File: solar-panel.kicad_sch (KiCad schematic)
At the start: 2 parts, among them U501 MCP3008

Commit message: solar panel init
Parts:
- renumbered U501 to U101
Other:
- added sheet Solar Cells (pv_cells.kicad_sch)
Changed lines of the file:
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@@
     (stroke (width 0) (type default))
-  )
-  (rectangle (start 102.87 53.34) (end 165.1 115.57)
-    (stroke (width 0) (type default))
-    (fill (type none))
   )
   (text "ADC\n" (at 118.11 71.12 0)
@@
   (symbol (lib_id "Analog_ADC:MCP3008") (at 129.54 91.44 0) (unit 1)
     (in_bom yes) (on_board yes) (dnp no) (fields_autoplaced)
-    (property "Reference" "U501" (at 124.3583 107.1499 0)
+    (property "Reference" "U101" (at 124.3583 107.1499 0)
       (effects (font (size 1.27 1.27)) (justify right))
     )
@@
       )
     )
+  )
+  (sheet (at 166.37 52.07) (size 35.56 5.08) (fields_autoplaced)
+    (stroke (width 0.1524) (type solid))
+    (fill (color 199 255 204 1.0000))
+    (property "Sheetname" "Solar Cells" (at 166.37 51.3584 0)
+      (effects (font (size 1.27 1.27)) (justify left bottom))
+    )
+    (property "Sheetfile" "pv_cells.kicad_sch" (at 166.37 57.7346 0)
+      (effects (font (size 1.27 1.27)) (justify left top))
+    )
+    (pin "PV_V+" output (at 201.93 54.61 0)
+      (effects (font (size 1.27 1.27)) (justify right))
+    )
+    (pin "PV_V-" input (at 166.37 54.61 180)
+      (effects (font (size 1.27 1.27)) (justify left))
+    )
+    (instances
+      (project "solar-panel"
+        (path "/3cfd2153-52bb-4eed-95c6-13d99c50d08a" (page "6"))
+      )
+    )

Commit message: rev 1.0, added pdf
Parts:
- added J101: Conn_01x10, Connector_PinSocket_1.00mm:PinSocket_1x10_P1.00mm_Vertical, symbol Connector_Generic:Conn_01x10
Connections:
- net MISO: now also J101.3 (Pin_3)
- net MOSI: now also J101.2 (Pin_2)
- net SCK: now also J101.1 (Pin_1)
- net Solar Cells/PV_V+: now also J101.10 (Pin_10), J101.8 (Pin_8), J101.9 (Pin_9)
- net Solar Cells/PV_V-: now also J101.5 (Pin_5), J101.6 (Pin_6), J101.7 (Pin_7)
- net ~{CS}: now also J101.4 (Pin_4)
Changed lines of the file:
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@@
 (kicad_sch (version 20230121) (generator eeschema)
   (paper "A4")
+  (junction (at 171.45 104.14) (diameter 0) (color 0 0 0 0)
+  )
   (junction (at 134.62 78.74) (diameter 0) (color 0 0 0 0)
   )
+  (junction (at 171.45 106.68) (diameter 0) (color 0 0 0 0)
+  )
   (junction (at 130.81 106.68) (diameter 0) (color 0 0 0 0)
+  )
+  (junction (at 171.45 109.22) (diameter 0) (color 0 0 0 0)
+  )
+  (junction (at 171.45 101.6) (diameter 0) (color 0 0 0 0)
   )
   (junction (at 134.62 63.5) (diameter 0) (color 0 0 0 0)
@@
   (no_connect (at 114.3 99.06))
   (no_connect (at 114.3 93.98))
-  (wire (pts (xy 149.86 96.52) (xy 144.78 96.52))
+  (wire (pts (xy 171.45 106.68) (xy 171.45 109.22))
+    (stroke (width 0) (type default))
+  )
+  (wire (pts (xy 144.78 96.52) (xy 171.45 96.52))
     (stroke (width 0) (type default))
   )
@@
     (stroke (width 0) (type default))
   )
+  (wire (pts (xy 144.78 88.9) (xy 171.45 88.9))
+    (stroke (width 0) (type default))
+  )
+  (wire (pts (xy 158.75 104.14) (xy 171.45 104.14))
+    (stroke (width 0) (type default))
+  )
   (wire (pts (xy 130.81 106.68) (xy 134.62 106.68))
     (stroke (width 0) (type default))
@@
     (stroke (width 0) (type default))
   )
+  (wire (pts (xy 171.45 109.22) (xy 171.45 111.76))
+    (stroke (width 0) (type default))
+  )
+  (wire (pts (xy 158.75 106.68) (xy 171.45 106.68))
+    (stroke (width 0) (type default))
+  )
   (wire (pts (xy 86.36 76.2) (xy 114.3 76.2))
     (stroke (width 0) (type default))
@@
     (stroke (width 0) (type default))
   )
-  (wire (pts (xy 149.86 88.9) (xy 144.78 88.9))
-    (stroke (width 0) (type default))
-  )
   (wire (pts (xy 134.62 63.5) (xy 139.7 63.5))
     (stroke (width 0) (type default))
   )
-  (wire (pts (xy 149.86 93.98) (xy 144.78 93.98))
+  (wire (pts (xy 144.78 93.98) (xy 171.45 93.98))
+    (stroke (width 0) (type default))
+  )
+  (wire (pts (xy 171.45 99.06) (xy 171.45 101.6))
+    (stroke (width 0) (type default))
+  )
+  (wire (pts (xy 171.45 101.6) (xy 171.45 104.14))
     (stroke (width 0) (type default))
   )
@@
     (stroke (width 0) (type default))
   )
-  (wire (pts (xy 149.86 91.44) (xy 144.78 91.44))
+  (wire (pts (xy 144.78 91.44) (xy 171.45 91.44))
     (stroke (width 0) (type default))
   )
@@
     )
   )
+  (symbol (lib_id "Connector_Generic:Conn_01x10") (at 176.53 99.06 0) (unit 1)
+    (in_bom yes) (on_board yes) (dnp no) (fields_autoplaced)
+    (property "Reference" "J101" (at 178.562 99.6863 0)
+      (effects (font (size 1.27 1.27)) (justify left))
+    )
+    (property "Value" "Conn_01x10" (at 178.562 101.6073 0)
+      (effects (font (size 1.27 1.27)) (justify left))
+    )
+    (property "Footprint" "Connector_PinSocket_1.00mm:PinSocket_1x10_P1.00mm_Vertical" (at 176.53 99.06 0)
+      (effects (font (size 1.27 1.27)) hide)
+    )
+    (property "Datasheet" "~" (at 176.53 99.06 0)
+      (effects (font (size 1.27 1.27)) hide)
+    )
+    (pin "1")
+    (pin "10")
+    (pin "2")
+    (pin "3")
+    (pin "4")
+    (pin "5")
+    (pin "6")
+    (pin "7")
+    (pin "8")
+    (pin "9")
+    (instances
+      (project "solar-panel"
+        (path "/3cfd2153-52bb-4eed-95c6-13d99c50d08a"
+          (reference "J101") (unit 1)
+        )
+      )
+    )
+  )
   (sheet (at 68.58 83.82) (size 17.78 4.699)
     (stroke (width 0.1524) (type solid))
@@
     )
   )
-  (sheet (at 166.37 52.07) (size 35.56 5.08) (fields_autoplaced)
+  (sheet (at 146.05 101.6) (size 12.7 7.62) (fields_autoplaced)
     (stroke (width 0.1524) (type solid))
     (fill (color 199 255 204 1.0000))
-    (property "Sheetname" "Solar Cells" (at 166.37 51.3584 0)
+    (property "Sheetname" "Solar Cells" (at 146.05 100.8884 0)
       (effects (font (size 1.27 1.27)) (justify left bottom))
     )
-    (property "Sheetfile" "pv_cells.kicad_sch" (at 166.37 57.7346 0)
+    (property "Sheetfile" "pv_cells.kicad_sch" (at 146.05 109.8046 0)
       (effects (font (size 1.27 1.27)) (justify left top))
     )
-    (pin "PV_V+" output (at 201.93 54.61 0)
-      (effects (font (size 1.27 1.27)) (justify right))
-    )
-    (pin "PV_V-" input (at 166.37 54.61 180)
-      (effects (font (size 1.27 1.27)) (justify left))
-    )
-    (instances
+    (pin "PV_V+" output (at 158.75 106.68 0)
+      (effects (font (size 1.27 1.27)) (justify right))
+    )
+    (pin "PV_V-" input (at 158.75 104.14 0)
+      (effects (font (size 1.27 1.27)) (justify right))
+    )
+    (instances

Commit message: rev 1.0 routed by Jonah
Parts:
- removed J101: Conn_01x10, Connector_PinSocket_1.00mm:PinSocket_1x10_P1.00mm_Vertical, symbol Connector_Generic:Conn_01x10
- added H101, H102, H103, H104, H105, H106: MountingHole, MountingHole:MountingHole_2.7mm, symbol Mechanical:MountingHole
- added J101: Conn_01x05_Pin, Connector_Hirose:Hirose_DF13-05P-1.25DSA_1x05_P1.25mm_Vertical, symbol Connector:Conn_01x05_Pin
- added J102: Conn_01x02, Connector_PinHeader_2.54mm:PinHeader_1x02_P2.54mm_Vertical, symbol Connector_Generic:Conn_01x02
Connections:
- net +3.3V: now also J101.5 (Pin_5)
- net GND: now also J102.2 (Pin_2)
- net MISO: now also J101.2 (Pin_2)
- net MOSI: now also J101.3 (Pin_3)
- net SCK: now also J101.4 (Pin_4)
- net Solar Cells/PV_V+: now also J102.1 (Pin_1)
- net ~{CS}: now also J101.1 (Pin_1)
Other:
- sheet Solar Cells ports: added none; removed PV_V-
- note added: "MOUNTING HOLES"
- moved on the sheet: C101, U101

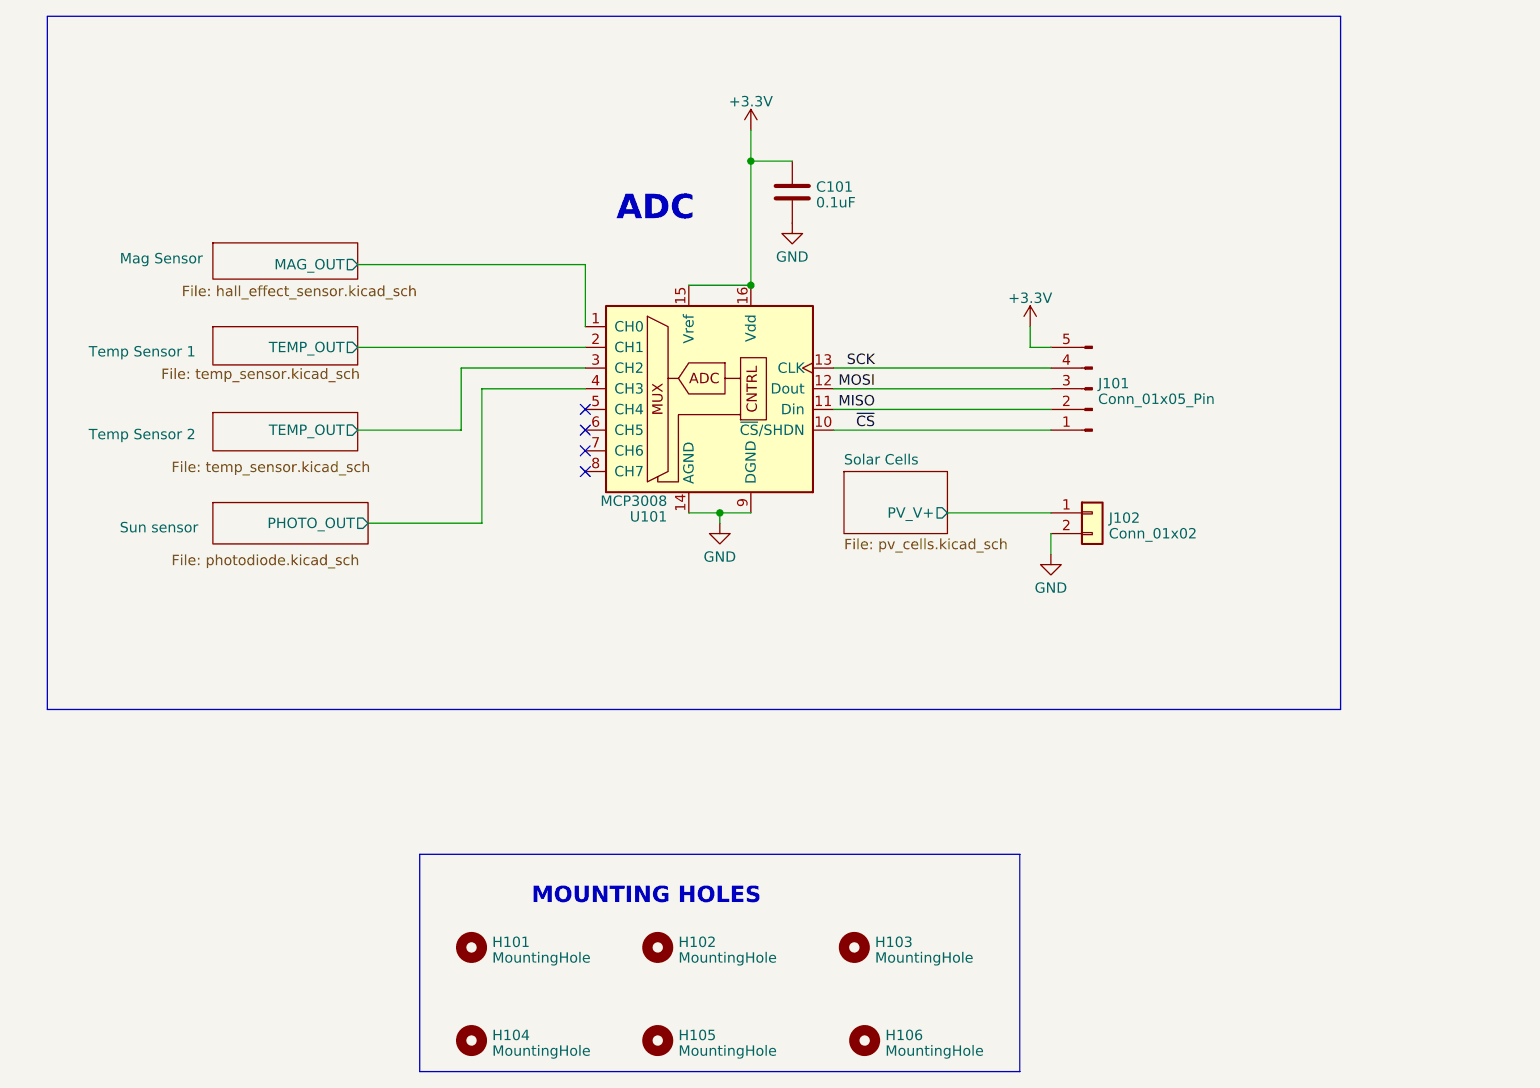
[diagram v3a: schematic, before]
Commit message: Remade schematic for all panels Fixed lightricity footprint Erased panel PCBs
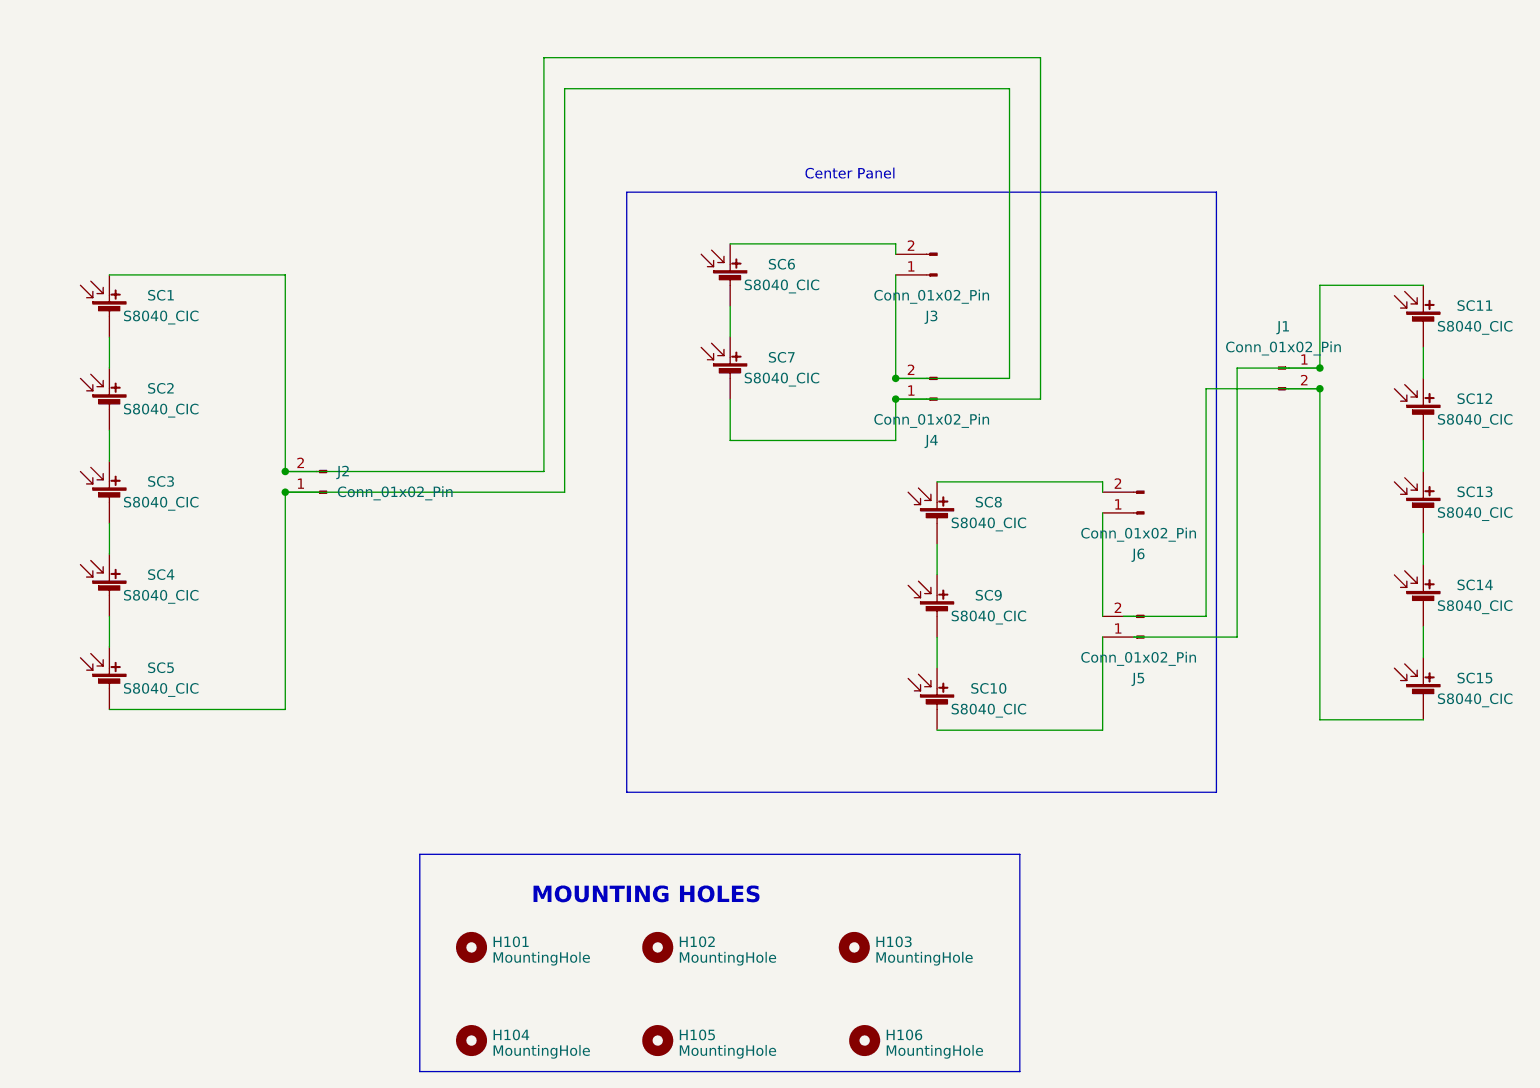
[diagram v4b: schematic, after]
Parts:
- removed C101: 0.1uF, Capacitor_SMD:C_0603_1608Metric_Pad1.08x0.95mm_HandSolder, symbol Device:C
- removed J101: Conn_01x05_Pin, Connector_Hirose:Hirose_DF13-05P-1.25DSA_1x05_P1.25mm_Vertical, symbol Connector:Conn_01x05_Pin
- removed J102: Conn_01x02, Connector_PinHeader_2.54mm:PinHeader_1x02_P2.54mm_Vertical, symbol Connector_Generic:Conn_01x02
- removed U101: MCP3008, Package_SO:SOIC-16_3.9x9.9mm_P1.27mm, symbol Analog_ADC:MCP3008
- added J1, J2, J3, J4, J5, J6: Conn_01x02_Pin, Connector_PinSocket_2.54mm:PinSocket_1x02_P2.54mm_Vertical, symbol Connector:Conn_01x02_Pin
- added SC1, SC10, SC11, SC12, SC13, SC14, SC15, SC2, SC3, SC4, SC5, SC6, SC7, SC8, SC9: S8040_CIC, Solar_cell:Solar_Cell_Lightricity_S8040_CIC, symbol Device:Solar_Cell
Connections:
- new net: J1.1 (Pin_1), SC11.1 (+)
- new net: SC11.2 (-), SC12.1 (+)
- new net: SC4.2 (-), SC5.1 (+)
- new net: J2.1 (Pin_1), J3.1 (Pin_1), J4.2 (Pin_2), SC5.2 (-)
- new net: SC12.2 (-), SC13.1 (+)
- new net: SC13.2 (-), SC14.1 (+)
- new net: J6.2 (Pin_2), SC8.1 (+)
- new net: SC8.2 (-), SC9.1 (+)
- new net: J1.2 (Pin_2), SC15.2 (-)
- new net: J5.2 (Pin_2), J6.1 (Pin_1)
- new net: J3.2 (Pin_2), SC6.1 (+)
- new net: SC14.2 (-), SC15.1 (+)
- new net: SC1.2 (-), SC2.1 (+)
- new net: SC2.2 (-), SC3.1 (+)
- new net: J2.2 (Pin_2), J4.1 (Pin_1), SC1.1 (+), SC7.2 (-)
- new net: SC6.2 (-), SC7.1 (+)
- new net: J5.1 (Pin_1), SC10.2 (-)
- new net: SC3.2 (-), SC4.1 (+)
- new net: SC10.1 (+), SC9.2 (-)
- no-connect marks 4 -> 0
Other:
- removed sheet Mag Sensor
- removed sheet Solar Cells
- removed sheet Sun sensor
- removed sheet Temp Sensor 1
- removed sheet Temp Sensor 2
- note added: "Center Panel"
- note removed: "ADC"

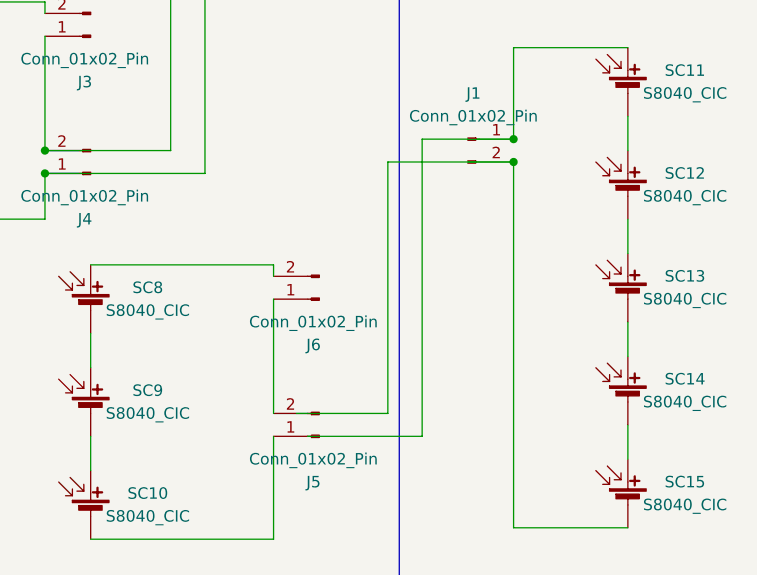
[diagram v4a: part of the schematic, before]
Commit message: rearanged panels, updated solar cells footprint
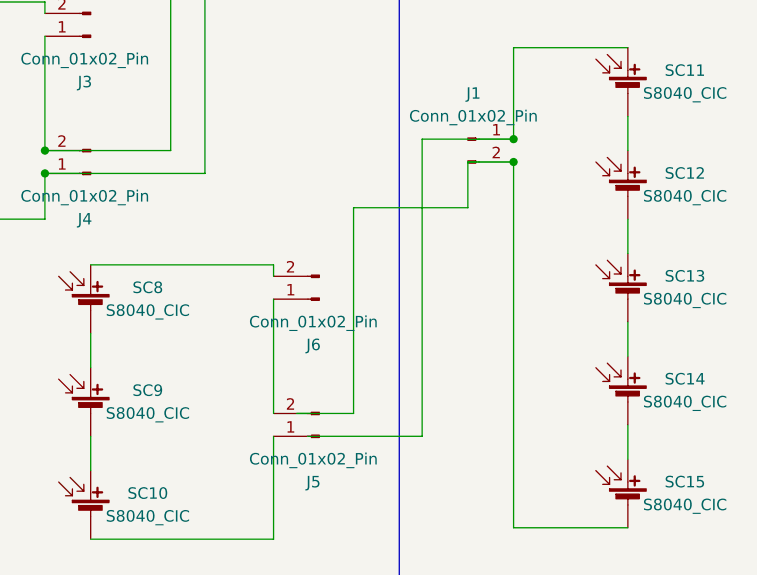
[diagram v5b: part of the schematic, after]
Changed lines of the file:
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@@
 	(wire
 		(pts
-			(xy 199.39 95.25) (xy 199.39 67.31)
+			(xy 195.58 95.25) (xy 195.58 72.39)
 		)
 		(stroke
@@
 	(wire
 		(pts
+			(xy 208.28 72.39) (xy 208.28 67.31)
+		)
+		(stroke
+			(width 0)
+			(type default)
+		)
+	)
+	(wire
+		(pts
 			(xy 175.26 30.48) (xy 120.65 30.48)
 		)
@@
 	(wire
 		(pts
-			(xy 199.39 67.31) (xy 213.36 67.31)
-		)
-		(stroke
-			(width 0)
-			(type default)
-		)
-	)
-	(wire
-		(pts
-			(xy 189.23 95.25) (xy 199.39 95.25)
+			(xy 195.58 72.39) (xy 208.28 72.39)
+		)
+		(stroke
+			(width 0)
+			(type default)
+		)
+	)
+	(wire
+		(pts
+			(xy 189.23 95.25) (xy 195.58 95.25)
 		)
 		(stroke
@@
 		)
 		(stroke
+			(width 0)
+			(type default)
+		)
+	)
+	(wire
+		(pts
+			(xy 208.28 67.31) (xy 213.36 67.31)
+		)
+		(stroke
